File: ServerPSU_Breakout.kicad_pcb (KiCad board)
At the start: 2 copper layers, 91.4 x 76.2 mm, 4 parts

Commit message: update
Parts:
- J_DATA1: value 1x10_2.54mm -> 2x5_2.54mm; footprint Connector_PinHeader_2.54mm:PinHeader_1x10_P2.54mm_Horizontal -> Connector_PinHeader_2.54mm:PinHeader_2x05_P2.54mm_Vertical; moved to B.Cu
- moved J_DATA1 20.0 mm to (189.2, 107.3), turned to 90 degrees
- moved J_GND1 2.54 mm to (190.5, 68.6)
- moved J_VOUT1 1.27 mm to (111.8, 68.6)
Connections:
- J_DATA1 pad 1: /ADDR -> /PSON
- J_DATA1 pad 10: /PSON -> /PSINTERRUPT
- J_DATA1 pad 2: /GND -> /ISHARE
- J_DATA1 pad 3: /SCL -> /SDA
- J_DATA1 pad 4: /SDA -> /PSOK
- J_DATA1 pad 5: /PSINTERRUPT -> /SCL
- J_DATA1 pad 6: /12VSB -> /PRESENT
- J_DATA1 pad 7: /PRESENT -> /ADDR
- J_DATA1 pad 8: /PSOK -> /12VSB
- J_DATA1 pad 9: /ISHARE -> /GND
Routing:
- net /ADDR: track 39.6 -> 11.1 mm
- net /SCL: track 27.2 -> 10.5 mm
- net /PSINTERRUPT: track 50.9 -> 65.9 mm
- net /SDA: track 23.6 -> 10.5 mm
- net /12VSB: track 42.7 -> 53.6 mm
- net /PRESENT: track 33.9 -> 41.6 mm
- net /PSOK: track 35.4 -> 42.3 mm
- net /PSON: track 11.5 -> 18.5 mm
- net /ISHARE: track 24.5 -> 28.9 mm
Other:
- board text added: "HSTNS_PL18 PSU Breakout RevA - Chris Sutton © 0819"

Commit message: RevB update
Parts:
- J_DATA1: footprint Connector_PinHeader_2.54mm:PinHeader_2x05_P2.54mm_Vertical -> Connector_PinHeader_2.54mm:PinHeader_2x05_P2.54mm_Horizontal; moved to F.Cu
- moved J_DATA1 16.0 mm to (189.2, 91.3), turned to 270 degrees
- moved J_GND1 3.81 mm to (190.5, 72.4)
- moved J_VOUT1 3.81 mm to (111.8, 72.4)
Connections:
- J_DATA1 pad 1: /PSON -> /ISHARE
- J_DATA1 pad 10: /PSINTERRUPT -> /GND
- J_DATA1 pad 2: /ISHARE -> /PSON
- J_DATA1 pad 3: /SDA -> /PSOK
- J_DATA1 pad 4: /PSOK -> /SDA
- J_DATA1 pad 5: /SCL -> /PRESENT
- J_DATA1 pad 6: /PRESENT -> /SCL
- J_DATA1 pad 7: /ADDR -> /12VSB
- J_DATA1 pad 8: /12VSB -> /ADDR
- J_DATA1 pad 9: /GND -> /PSINTERRUPT
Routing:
- net /PRESENT: track 41.6 -> 56.8 mm
- net /SCL: track 10.5 -> 24.6 mm
- net /SDA: track 10.5 -> 24.5 mm
- net /ADDR: track 11.1 -> 24.6 mm
- net /12VSB: track 53.6 -> 65.3 mm
- net /PSON: track 18.5 -> 29.9 mm
- net /ISHARE: track 28.9 -> 39.5 mm
- net /PSINTERRUPT: track 65.9 -> 76.4 mm
- net /PSOK: track 42.3 -> 49.7 mm
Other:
- board size 91.4 x 76.2 mm -> 91.4 x 69.8 mm
- board text added: "HSTNS_PL18 PSU Breakout RevB - Chris Sutton © 1019"
- board text removed: "HSTNS_PL18 PSU Breakout RevA - Chris Sutton © 0819"

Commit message: updated design
- corrected control pins
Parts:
- J_PSU_IN1: moved to F.Cu
- moved J_DATA1 6.35 mm to (182.9, 91.3)
- turned J_PSU_IN1 to 90 degrees
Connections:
- J_PSU_IN1 pad 28: (no net) -> Net-(J_PSU_IN1-Pad28)
- J_PSU_IN1 pad 29: (no net) -> Net-(J_PSU_IN1-Pad29)
- J_PSU_IN1 pad 31: /SCL -> /SDA
- J_PSU_IN1 pad 32: /SDA -> /SCL
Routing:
- net /ADDR: track 24.6 -> 56.1 mm
- net /SDA: track 24.5 -> 51.4 mm
- net /SCL: track 24.6 -> 44.1 mm
- net /12VSB: track 65.3 -> 71.7 mm
- net /PRESENT: track 56.8 -> 62.8 mm
- net /PSOK: track 49.7 -> 53.4 mm
- net /PSON: track 29.9 -> 33.5 mm
- net /PSINTERRUPT: track 76.4 -> 79.7 mm
- net /ISHARE: track 39.5 -> 42.0 mm

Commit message: updates
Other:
- board text added: "HSTNS_PL18 PSU Breakout RevC - Chris Sutton © 0120"
- board text removed: "HSTNS_PL18 PSU Breakout RevB - Chris Sutton © 1019"
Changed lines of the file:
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@@
   )
   (setup
-    (last_trace_width 0.4)
+    (last_trace_width 0.25)
     (user_trace_width 0.4)
     (user_trace_width 0.5)
@@
     )
   )
-  (gr_circle (center 163.87 96.647) (end 164.505 96.647) (layer B.SilkS) (width 0.2))
-  (gr_circle (center 158.75 96.647) (end 159.385 96.647) (layer B.SilkS) (width 0.2))
-  (gr_line (start 170.815 100.838) (end 156.845 100.838) (layer B.SilkS) (width 0.2))
-  (gr_line (start 170.815 95.123) (end 170.815 100.838) (layer B.SilkS) (width 0.2))
-  (gr_line (start 156.845 100.838) (end 156.845 95.123) (layer B.SilkS) (width 0.2))
-  (gr_circle (center 161.31 99.207) (end 161.945 99.207) (layer B.SilkS) (width 0.2))
-  (gr_circle (center 158.75 99.207) (end 159.385 99.207) (layer B.SilkS) (width 0.2))
-  (gr_circle (center 163.87 99.207) (end 164.505 99.207) (layer B.SilkS) (width 0.2))
-  (gr_circle (center 166.43 99.207) (end 167.065 99.207) (layer B.SilkS) (width 0.2))
-  (gr_line (start 156.845 95.123) (end 170.815 95.123) (layer B.SilkS) (width 0.2))
-  (gr_circle (center 166.43 96.647) (end 167.065 96.647) (layer B.SilkS) (width 0.2))
-  (gr_circle (center 168.99 96.647) (end 169.625 96.647) (layer B.SilkS) (width 0.2))
-  (gr_circle (center 161.31 96.647) (end 161.945 96.647) (layer B.SilkS) (width 0.2))
-  (gr_circle (center 168.99 99.207) (end 169.625 99.207) (layer B.SilkS) (width 0.2))
-  (gr_circle (center 168.99 99.207) (end 168.99 99.842) (layer F.SilkS) (width 0.2))
-  (gr_circle (center 166.43 99.207) (end 166.43 99.842) (layer F.SilkS) (width 0.2))
-  (gr_circle (center 163.87 99.207) (end 163.87 99.842) (layer F.SilkS) (width 0.2))
-  (gr_circle (center 161.31 99.207) (end 161.31 99.842) (layer F.SilkS) (width 0.2))
-  (gr_circle (center 158.75 99.207) (end 158.75 99.842) (layer F.SilkS) (width 0.2))
-  (gr_circle (center 168.99 96.647) (end 168.99 97.282) (layer F.SilkS) (width 0.2))
-  (gr_circle (center 166.43 96.647) (end 166.43 97.282) (layer F.SilkS) (width 0.2))
-  (gr_circle (center 163.87 96.647) (end 163.87 97.282) (layer F.SilkS) (width 0.2))
-  (gr_circle (center 161.31 96.647) (end 161.31 97.282) (layer F.SilkS) (width 0.2))
-  (gr_circle (center 158.75 96.647) (end 158.75 97.282) (layer F.SilkS) (width 0.2))
-  (gr_line (start 156.845 100.838) (end 156.845 95.123) (layer F.SilkS) (width 0.2))
-  (gr_line (start 170.815 100.838) (end 156.845 100.838) (layer F.SilkS) (width 0.2))
-  (gr_line (start 170.815 95.123) (end 170.815 100.838) (layer F.SilkS) (width 0.2))
-  (gr_line (start 156.845 95.123) (end 170.815 95.123) (layer F.SilkS) (width 0.2))
-  (gr_text "HSTNS_PL18 PSU Breakout RevB - Chris Sutton © 1019" (at 141.605 111.76) (layer F.SilkS)
+  (gr_circle (center 161.33 91.186) (end 161.965 91.186) (layer B.SilkS) (width 0.2))
+  (gr_circle (center 156.21 91.186) (end 156.845 91.186) (layer B.SilkS) (width 0.2))
+  (gr_line (start 168.275 95.377) (end 154.305 95.377) (layer B.SilkS) (width 0.2))
+  (gr_line (start 168.275 89.662) (end 168.275 95.377) (layer B.SilkS) (width 0.2))
+  (gr_line (start 154.305 95.377) (end 154.305 89.662) (layer B.SilkS) (width 0.2))
+  (gr_circle (center 158.77 93.746) (end 159.405 93.746) (layer B.SilkS) (width 0.2))
+  (gr_circle (center 156.21 93.746) (end 156.845 93.746) (layer B.SilkS) (width 0.2))
+  (gr_circle (center 161.33 93.746) (end 161.965 93.746) (layer B.SilkS) (width 0.2))
+  (gr_circle (center 163.89 93.746) (end 164.525 93.746) (layer B.SilkS) (width 0.2))
+  (gr_line (start 154.305 89.662) (end 168.275 89.662) (layer B.SilkS) (width 0.2))
+  (gr_circle (center 163.89 91.186) (end 164.525 91.186) (layer B.SilkS) (width 0.2))
+  (gr_circle (center 166.45 91.186) (end 167.085 91.186) (layer B.SilkS) (width 0.2))
+  (gr_circle (center 158.77 91.186) (end 159.405 91.186) (layer B.SilkS) (width 0.2))
+  (gr_circle (center 166.45 93.746) (end 167.085 93.746) (layer B.SilkS) (width 0.2))
+  (gr_circle (center 166.45 93.746) (end 166.45 94.381) (layer F.SilkS) (width 0.2))
+  (gr_circle (center 163.89 93.746) (end 163.89 94.381) (layer F.SilkS) (width 0.2))
+  (gr_circle (center 161.33 93.746) (end 161.33 94.381) (layer F.SilkS) (width 0.2))
+  (gr_circle (center 158.77 93.746) (end 158.77 94.381) (layer F.SilkS) (width 0.2))
+  (gr_circle (center 156.21 93.746) (end 156.21 94.381) (layer F.SilkS) (width 0.2))
+  (gr_circle (center 166.45 91.186) (end 166.45 91.821) (layer F.SilkS) (width 0.2))
+  (gr_circle (center 163.89 91.186) (end 163.89 91.821) (layer F.SilkS) (width 0.2))
+  (gr_circle (center 161.33 91.186) (end 161.33 91.821) (layer F.SilkS) (width 0.2))
+  (gr_circle (center 158.77 91.186) (end 158.77 91.821) (layer F.SilkS) (width 0.2))
+  (gr_circle (center 156.21 91.186) (end 156.21 91.821) (layer F.SilkS) (width 0.2))
+  (gr_line (start 154.305 95.377) (end 154.305 89.662) (layer F.SilkS) (width 0.2))
+  (gr_line (start 168.275 95.377) (end 154.305 95.377) (layer F.SilkS) (width 0.2))
+  (gr_line (start 168.275 89.662) (end 168.275 95.377) (layer F.SilkS) (width 0.2))
+  (gr_line (start 154.305 89.662) (end 168.275 89.662) (layer F.SilkS) (width 0.2))
+  (gr_text "HSTNS_PL18 PSU Breakout RevC - Chris Sutton © 0120" (at 141.605 111.76) (layer F.SilkS)
     (effects (font (size 1.5 1.5) (thickness 0.3)))
   )
-  (gr_text "HSTNS_PL18 PSU Breakout RevB - Chris Sutton © 1019" (at 141.605 111.76) (layer B.SilkS)
+  (gr_text "HSTNS_PL18 PSU Breakout RevC - Chris Sutton © 0120" (at 141.605 111.76) (layer B.SilkS)
     (effects (font (size 1.5 1.5) (thickness 0.3)) (justify mirror))
   )
-  (gr_text ADDR (at 161.417 101.378622 90) (layer B.SilkS)
+  (gr_text ADDR (at 158.877 95.917622 90) (layer B.SilkS)
     (effects (font (size 1.2 1.2) (thickness 0.1)) (justify left mirror))
   )
-  (gr_text SDA (at 166.497 101.378622 90) (layer B.SilkS)
+  (gr_text SDA (at 163.957 95.917622 90) (layer B.SilkS)
     (effects (font (size 1.2 1.2) (thickness 0.1)) (justify left mirror))
   )
-  (gr_text PSINT (at 158.753445 94.534561 90) (layer B.SilkS)
+  (gr_text PSINT (at 156.213445 89.073561 90) (layer B.SilkS)
     (effects (font (size 1.2 1.2) (thickness 0.1)) (justify right mirror))
   )
-  (gr_text SCL (at 163.957 101.378622 90) (layer B.SilkS)
+  (gr_text SCL (at 161.417 95.917622 90) (layer B.SilkS)
     (effects (font (size 1.2 1.2) (thickness 0.1)) (justify left mirror))
   )
-  (gr_text ISHARE (at 168.893784 94.309036 90) (layer B.SilkS)
+  (gr_text ISHARE (at 166.497 89.027 90) (layer B.SilkS)
     (effects (font (size 1.2 1.2) (thickness 0.1)) (justify right mirror))
   )
-  (gr_text PRES (at 163.833445 94.534561 90) (layer B.SilkS)
+  (gr_text PRES (at 161.293445 89.073561 90) (layer B.SilkS)
     (effects (font (size 1.2 1.2) (thickness 0.1)) (justify right mirror))
   )
-  (gr_text PSOK (at 166.373445 94.534561 90) (layer B.SilkS)
+  (gr_text PSOK (at 163.833445 89.073561 90) (layer B.SilkS)
     (effects (font (size 1.2 1.2) (thickness 0.1)) (justify right mirror))
   )
-  (gr_text PSON (at 169.037 101.378622 90) (layer B.SilkS)
+  (gr_text PSON (at 166.497 95.917622 90) (layer B.SilkS)
     (effects (font (size 1.2 1.2) (thickness 0.1)) (justify left mirror))
   )
-  (gr_text 12VSB (at 161.293445 88.819561 90) (layer B.SilkS)
+  (gr_text 12VSB (at 158.753445 83.358561 90) (layer B.SilkS)
     (effects (font (size 1.2 1.2) (thickness 0.1)) (justify left mirror))
   )
-  (gr_text GND (at 158.877 101.378622 90) (layer B.SilkS)
+  (gr_text GND (at 156.337 95.917622 90) (layer B.SilkS)
     (effects (font (size 1.2 1.2) (thickness 0.1)) (justify left mirror))
   )
-  (gr_text PSON (at 169.037 101.378622 90) (layer F.SilkS)
+  (gr_text PSON (at 166.497 95.917622 90) (layer F.SilkS)
     (effects (font (size 1.2 1.2) (thickness 0.1)) (justify right))
   )
-  (gr_text ISHARE (at 169.020784 94.436036 90) (layer F.SilkS)
+  (gr_text ISHARE (at 166.480784 88.975036 90) (layer F.SilkS)
     (effects (font (size 1.2 1.2) (thickness 0.1)) (justify left))
   )
-  (gr_text PSOK (at 166.373445 94.407561 90) (layer F.SilkS)
+  (gr_text PSOK (at 163.833445 88.946561 90) (layer F.SilkS)
     (effects (font (size 1.2 1.2) (thickness 0.1)) (justify left))
   )
-  (gr_text PRES (at 163.833445 94.407561 90) (layer F.SilkS)
+  (gr_text PRES (at 161.293445 88.946561 90) (layer F.SilkS)
     (effects (font (size 1.2 1.2) (thickness 0.1)) (justify left))
   )
-  (gr_text 12VSB (at 161.293445 94.407561 90) (layer F.SilkS)
+  (gr_text 12VSB (at 158.753445 88.946561 90) (layer F.SilkS)
     (effects (font (size 1.2 1.2) (thickness 0.1)) (justify left))
   )
-  (gr_text PSINT (at 158.753445 94.407561 90) (layer F.SilkS)
+  (gr_text PSINT (at 156.213445 88.946561 90) (layer F.SilkS)
     (effects (font (size 1.2 1.2) (thickness 0.1)) (justify left))
   )
-  (gr_text SDA (at 166.497 101.378622 90) (layer F.SilkS)
+  (gr_text SDA (at 163.957 95.917622 90) (layer F.SilkS)
     (effects (font (size 1.2 1.2) (thickness 0.1)) (justify right))
   )
-  (gr_text SCL (at 163.957 101.378622 90) (layer F.SilkS)
+  (gr_text SCL (at 161.417 95.917622 90) (layer F.SilkS)
     (effects (font (size 1.2 1.2) (thickness 0.1)) (justify right))
   )
-  (gr_text GND (at 158.877 101.378622 90) (layer F.SilkS)
+  (gr_text GND (at 156.337 95.917622 90) (layer F.SilkS)
     (effects (font (size 1.2 1.2) (thickness 0.1)) (justify right))
   )
-  (gr_text ADDR (at 161.417 101.378622 90) (layer F.SilkS)
+  (gr_text ADDR (at 158.877 95.917622 90) (layer F.SilkS)
     (effects (font (size 1.2 1.2) (thickness 0.1)) (justify right))
   )

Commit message: layout draft
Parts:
- removed J_DATA1: 2x5_2.54mm, Connector_PinHeader_2.54mm:PinHeader_2x05_P2.54mm_Horizontal
- removed J_GND1, J_VOUT1: 1x6_5.08mm, Samtec HPM-06-02-T-S-RA_1x6:Samtec HPM-06-02-T-S-RA_2x6
- added C1: 100nF, Capacitor_SMD:C_0805_2012Metric_Pad1.15x1.40mm_HandSolder, B.Cu at (148.3, 68.7)
- added C2: 100nF, Capacitor_SMD:C_0805_2012Metric_Pad1.15x1.40mm_HandSolder, F.Cu at (166.1, 61.6)
- added C3: 100nF, Capacitor_SMD:C_0805_2012Metric_Pad1.15x1.40mm_HandSolder, F.Cu at (173.0, 70.5)
- added C4: 100nF, Capacitor_SMD:C_0805_2012Metric_Pad1.15x1.40mm_HandSolder, F.Cu at (174.0, 80.0)
- added C5: 100nF, Capacitor_SMD:C_0805_2012Metric_Pad1.15x1.40mm_HandSolder, F.Cu at (160.0, 84.5)
- added C6: 100nF, Capacitor_SMD:C_0805_2012Metric_Pad1.15x1.40mm_HandSolder, F.Cu at (160.0, 61.6)
- added J1: Conn_01x05, Connector_PinHeader_2.54mm:PinHeader_1x05_P2.54mm_Vertical, B.Cu at (116.8, 61.0)
- added J2: Conn_01x14, Connector_PinHeader_2.54mm:PinHeader_1x14_P2.54mm_Vertical, F.Cu at (203.3, 69.7)
- added J3: Conn_01x01, MountingHole:MountingHole_6.4mm_M6, F.Cu at (141.6, 131.3)
- added J4: Conn_01x01, MountingHole:MountingHole_6.4mm_M6, F.Cu at (181.7, 131.3)
- added L1: BEAD, Inductor_SMD:L_0805_2012Metric_Pad1.15x1.40mm_HandSolder, F.Cu at (163.8, 61.6)
- added Q1: DMG2302U, Package_TO_SOT_SMD:SOT-23, F.Cu at (205.5, 120.9)
- added R1: 10K, Resistor_SMD:R_0805_2012Metric_Pad1.15x1.40mm_HandSolder, B.Cu at (148.3, 75.1)
- added R2: 10K, Resistor_SMD:R_0805_2012Metric_Pad1.15x1.40mm_HandSolder, B.Cu at (148.3, 73.0)
- added R3: 22K, Resistor_SMD:R_0805_2012Metric_Pad1.15x1.40mm_HandSolder, B.Cu at (192.2, 124.7)
- added R4: 10K, Resistor_SMD:R_0805_2012Metric_Pad1.15x1.40mm_HandSolder, B.Cu at (148.3, 70.9)
- added REF**: MountingHole_6.4mm_M6, MountingHole:MountingHole_6.4mm_M6, F.Cu at (215.6, 86.2)
- added REF**: MountingHole_6.4mm_M6, MountingHole:MountingHole_6.4mm_M6, F.Cu at (107.6, 86.2)
- added REF**: MountingHole_6.4mm_M6, MountingHole:MountingHole_6.4mm_M6, F.Cu at (200.3, 130.8)
- added REF**: MountingHole_6.4mm_M6, MountingHole:MountingHole_6.4mm_M6, F.Cu at (123.1, 130.7)
- added REF**: MountingHole_6.4mm_M6, MountingHole:MountingHole_6.4mm_M6, F.Cu at (200.4, 52.8)
- added REF**: MountingHole_6.4mm_M6, MountingHole:MountingHole_6.4mm_M6, F.Cu at (123.2, 52.8)
- added U1: NCS1S1203SC, Converter_DCDC:Converter_DCDC_Murata_NCS1SxxxxSC_THT, B.Cu at (162.6, 108.6)
- added U2: STM32F072RBTx, Package_QFP:LQFP-64_10x10mm_P0.5mm, B.Cu at (163.8, 74.3)
- J_PSU_IN1: moved to B.Cu
- moved J_PSU_IN1 10.7 mm to (161.7, 117.3), turned to 270 degrees
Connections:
- net /12V renamed /OutputConnectors/PSU_VBUS
- net /GND renamed GNDS
- J_PSU_IN1 pad 27: /ADDR -> /PSUConnector/PSU_ADDR2
- J_PSU_IN1 pad 28: Net-(J_PSU_IN1-Pad28) -> /PSUConnector/PSU_ADDR1
- J_PSU_IN1 pad 29: Net-(J_PSU_IN1-Pad29) -> /PSUConnector/PSU_ADDR0
- J_PSU_IN1 pad 31: /SDA -> /PSUConnector/PSU_SDA
- J_PSU_IN1 pad 32: /SCL -> /PSUConnector/PSU_SCL
- J_PSU_IN1 pad 33: /PSON -> /HighVoltageControl/PSU_ON
- J_PSU_IN1 pad 34: /ISHARE -> /MCU/MCU_IMON
- J_PSU_IN1 pad 35: /PSOK -> /MCU/MCU_PSOK
- J_PSU_IN1 pad 36: /PRESENT -> /HighVoltageControl/PSU_PRES
- J_PSU_IN1 pad 37: /12VSB -> /HighVoltageControl/PSU_12VSB
- J_PSU_IN1 pad 38: /PSINTERRUPT -> /PSUConnector/PSU_INT
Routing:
- net /HighVoltageControl/MCU_3V3: track 0.00 -> 193.4 mm, vias 0 -> 7
- net /MCU/MCU_PSOK: track 0.00 -> 126.2 mm, vias 0 -> 1
- net /MCU/MCU_IMON: track 0.00 -> 119.4 mm, vias 0 -> 1
- net /PSUConnector/PSU_INT: track 0.00 -> 106.6 mm, vias 0 -> 1
- net /HighVoltageControl/MCU_SW: track 0.00 -> 97.2 mm, vias 0 -> 1
- net /PSUConnector/PSU_SCL: track 0.00 -> 93.3 mm, vias 0 -> 1
- net /PSUConnector/PSU_SDA: track 0.00 -> 92.7 mm, vias 0 -> 1
- net /PSINTERRUPT: track 79.7 -> 0.00 mm
- net /12VSB: track 71.7 -> 0.00 mm
- net /HighVoltageControl/PSU_12VSB: track 0.00 -> 69.4 mm, vias 0 -> 1
- net /PRESENT: track 62.8 -> 0.00 mm
- net /ADDR: track 56.1 -> 0.00 mm
- net /MCU/T_OUT: track 0.00 -> 54.2 mm
- net /MCU/T_IRQ: track 0.00 -> 53.7 mm, vias 0 -> 1
- net /PSOK: track 53.4 -> 0.00 mm
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- added copper zone on B.Cu, net /HighVoltageControl/MCU_GND
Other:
- board size 91.4 x 69.8 mm -> 120 x 90 mm
- net class Default: clearance 0.2 -> 0.127; trace_width 0.25 -> 0.127; via_dia 0.8 -> 0.6; via_drill 0.4 -> 0.3
- rule trace_clearance: 0.2 -> 0.127
- rule trace_min: 0.2 -> 0.127
- rule via_min_size: 0.4 -> 0.6
- board text removed: "12VSB"
- board text removed: "ADDR"
- board text removed: "GND"
- board text removed: "HSTNS_PL18 PSU Breakout RevC - Chris Sutton © 0120"
- board text removed: "ISHARE"
- board text removed: "PRES"
- board text removed: "PSINT"
- board text removed: "PSOK"
- board text removed: "PSON"
- board text removed: "SCL"
- board text removed: "SDA"

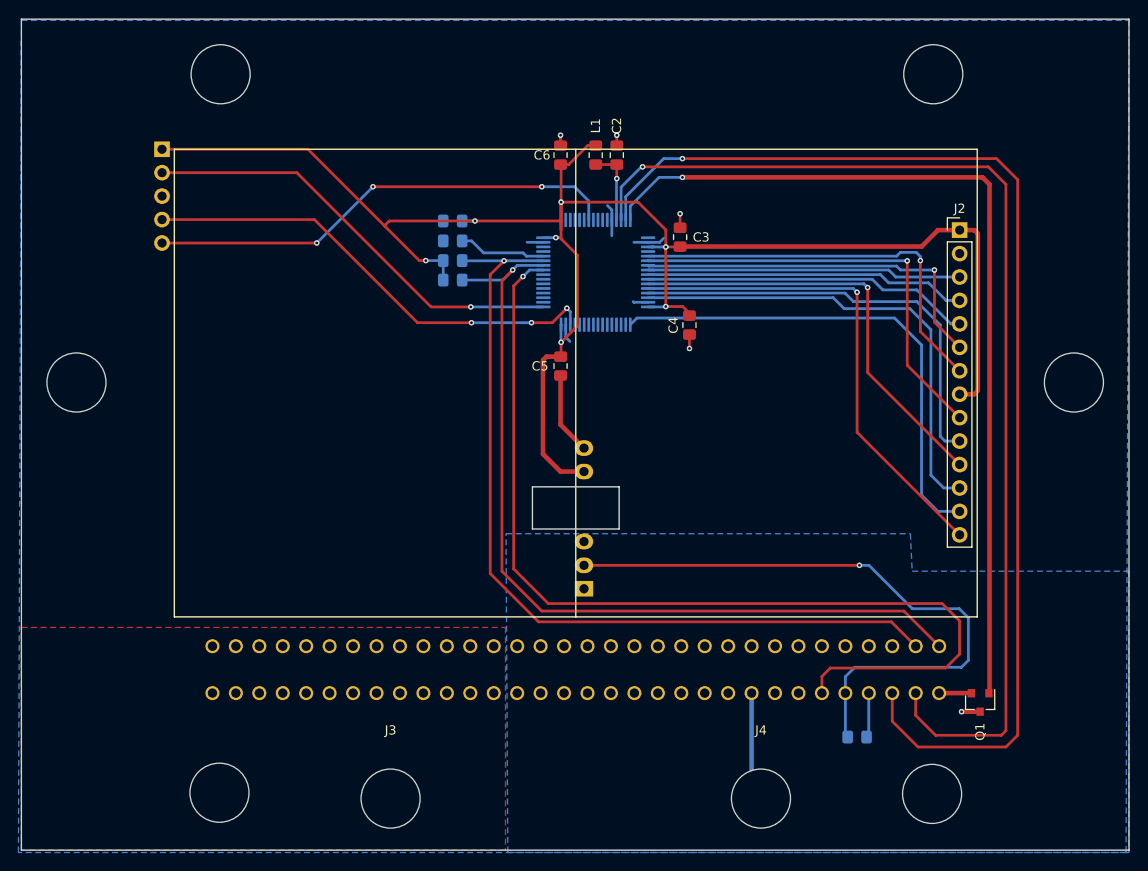
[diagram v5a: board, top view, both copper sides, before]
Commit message: moved SPI2 traces on MCU
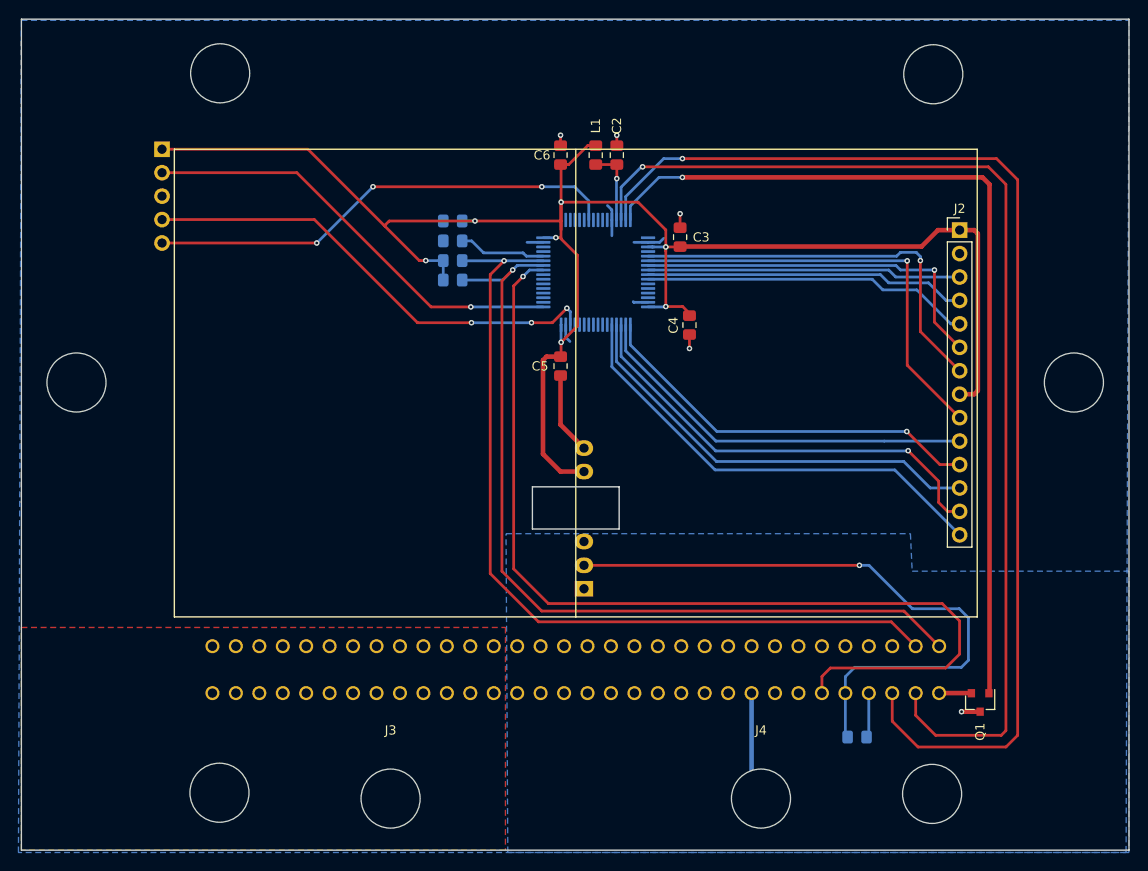
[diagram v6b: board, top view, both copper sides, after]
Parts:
- moved REF** 0.11 mm to (123.1, 52.7)
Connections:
- U2 pad 27: /MCU/T_CS -> Net-(U2-Pad27)
- U2 pad 28: /MCU/T_IRQ -> Net-(U2-Pad28)
- U2 pad 29: /MCU/T_CLK -> Net-(U2-Pad29)
- U2 pad 30: /MCU/T_DIN -> Net-(U2-Pad30)
- U2 pad 33: /MCU/T_OUT -> /MCU/T_CS
- U2 pad 34: Net-(U2-Pad34) -> /MCU/T_CLK
- U2 pad 35: Net-(U2-Pad35) -> /MCU/T_OUT
- U2 pad 36: Net-(U2-Pad36) -> /MCU/T_DIN
- U2 pad 37: Net-(U2-Pad37) -> /MCU/T_IRQ
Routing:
- net /MCU/T_OUT: track 54.2 -> 48.4 mm, vias 0 -> 1
- net /MCU/T_DIN: track 51.5 -> 46.9 mm
- net /MCU/T_CLK: track 47.5 -> 43.1 mm
- net /MCU/T_CS: track 47.3 -> 43.2 mm
- net /MCU/T_IRQ: track 53.7 -> 49.8 mm, vias 1 -> 0
